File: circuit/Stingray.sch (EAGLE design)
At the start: 14 parts, among them IC1 4052N, IC2 4052N, K1 5200, K3 PN87520-S, M1 ARDUINO-NANO-3.0

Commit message: added files via upload
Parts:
- added R6, R7, R8: 10k, rcl:R-EU_0204/7
- added X2: (no value), con-yamaichi:MD06SS
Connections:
- removed net TXD/SPARE: M1.D1/TX
- new net PS2CLK: M1.D1/TX, R6.2, X2.5
- new net PS2DAT: M1.D0/RX, R7.2, X2.1
- net +5V: now also R6.1, R7.1, R8.2, X2.4
- net DETECT: now also M1.A6, R8.1; no longer M1.D0/RX
- net GND: now also X2.3
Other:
- moved on the sheet: K2, K3

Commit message: Alpha release, Joystick control seems fine, keyboard emulation to be tested.
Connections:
- net BOTTOM: now also K1.13, M1.D3; no longer K1.14, M1.D2
- net TOP: now also K1.14, M1.D2; no longer K1.13, M1.D3
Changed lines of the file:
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@@
 <grid distance="0.1" unitdist="inch" unit="inch" style="lines" multiple="1" display="no" altdistance="0.01" altunitdist="inch" altunit="inch"/>
 <layers>
-<layer number="1" name="Top" color="4" fill="1" visible="yes" active="no"/>
-<layer number="16" name="Bottom" color="1" fill="1" visible="yes" active="no"/>
-<layer number="17" name="Pads" color="2" fill="1" visible="yes" active="no"/>
-<layer number="18" name="Vias" color="2" fill="1" visible="yes" active="no"/>
-<layer number="19" name="Unrouted" color="6" fill="1" visible="yes" active="no"/>
-<layer number="20" name="Dimension" color="15" fill="1" visible="yes" active="no"/>
-<layer number="21" name="tPlace" color="7" fill="1" visible="yes" active="no"/>
-<layer number="22" name="bPlace" color="7" fill="1" visible="yes" active="no"/>
-<layer number="23" name="tOrigins" color="15" fill="1" visible="yes" active="no"/>
-<layer number="24" name="bOrigins" color="15" fill="1" visible="yes" active="no"/>
-<layer number="25" name="tNames" color="7" fill="1" visible="yes" active="no"/>
-<layer number="26" name="bNames" color="7" fill="1" visible="yes" active="no"/>
-<layer number="27" name="tValues" color="7" fill="1" visible="yes" active="no"/>
-<layer number="28" name="bValues" color="7" fill="1" visible="yes" active="no"/>
+<layer number="1" name="Top" color="4" fill="1" visible="no" active="no"/>
+<layer number="16" name="Bottom" color="1" fill="1" visible="no" active="no"/>
+<layer number="17" name="Pads" color="2" fill="1" visible="no" active="no"/>
+<layer number="18" name="Vias" color="2" fill="1" visible="no" active="no"/>
+<layer number="19" name="Unrouted" color="6" fill="1" visible="no" active="no"/>
+<layer number="20" name="Dimension" color="15" fill="1" visible="no" active="no"/>
+<layer number="21" name="tPlace" color="7" fill="1" visible="no" active="no"/>
+<layer number="22" name="bPlace" color="7" fill="1" visible="no" active="no"/>
+<layer number="23" name="tOrigins" color="15" fill="1" visible="no" active="no"/>
+<layer number="24" name="bOrigins" color="15" fill="1" visible="no" active="no"/>
+<layer number="25" name="tNames" color="7" fill="1" visible="no" active="no"/>
+<layer number="26" name="bNames" color="7" fill="1" visible="no" active="no"/>
+<layer number="27" name="tValues" color="7" fill="1" visible="no" active="no"/>
+<layer number="28" name="bValues" color="7" fill="1" visible="no" active="no"/>
 <layer number="29" name="tStop" color="7" fill="3" visible="no" active="no"/>
 <layer number="30" name="bStop" color="7" fill="6" visible="no" active="no"/>
@@
 <layer number="35" name="tGlue" color="7" fill="4" visible="no" active="no"/>
 <layer number="36" name="bGlue" color="7" fill="5" visible="no" active="no"/>
-<layer number="37" name="tTest" color="7" fill="1" visible="yes" active="no"/>
-<layer number="38" name="bTest" color="7" fill="1" visible="yes" active="no"/>
+<layer number="37" name="tTest" color="7" fill="1" visible="no" active="no"/>
+<layer number="38" name="bTest" color="7" fill="1" visible="no" active="no"/>
 <layer number="39" name="tKeepout" color="4" fill="11" visible="no" active="no"/>
 <layer number="40" name="bKeepout" color="1" fill="11" visible="no" active="no"/>
@@
 <layer number="44" name="Drills" color="7" fill="1" visible="no" active="no"/>
 <layer number="45" name="Holes" color="7" fill="1" visible="no" active="no"/>
-<layer number="46" name="Milling" color="3" fill="1" visible="yes" active="no"/>
-<layer number="47" name="Measures" color="7" fill="1" visible="yes" active="no"/>
-<layer number="48" name="Document" color="7" fill="1" visible="yes" active="no"/>
-<layer number="49" name="Reference" color="7" fill="1" visible="yes" active="no"/>
-<layer number="50" name="dxf" color="7" fill="1" visible="yes" active="no"/>
-<layer number="51" name="tDocu" color="7" fill="1" visible="yes" active="no"/>
-<layer number="52" name="bDocu" color="7" fill="1" visible="yes" active="no"/>
-<layer number="53" name="tGND_GNDA" color="7" fill="9" visible="yes" active="no"/>
-<layer number="54" name="bGND_GNDA" color="1" fill="9" visible="yes" active="no"/>
-<layer number="56" name="wert" color="7" fill="1" visible="yes" active="no"/>
-<layer number="57" name="tCAD" color="7" fill="1" visible="yes" active="no"/>
-<layer number="59" name="tCarbon" color="7" fill="1" visible="yes" active="no"/>
-<layer number="60" name="bCarbon" color="7" fill="1" visible="yes" active="no"/>
+<layer number="46" name="Milling" color="3" fill="1" visible="no" active="no"/>
+<layer number="47" name="Measures" color="7" fill="1" visible="no" active="no"/>
+<layer number="48" name="Document" color="7" fill="1" visible="no" active="no"/>
+<layer number="49" name="Reference" color="7" fill="1" visible="no" active="no"/>
+<layer number="50" name="dxf" color="7" fill="1" visible="no" active="no"/>
+<layer number="51" name="tDocu" color="7" fill="1" visible="no" active="no"/>
+<layer number="52" name="bDocu" color="7" fill="1" visible="no" active="no"/>
+<layer number="53" name="tGND_GNDA" color="7" fill="9" visible="no" active="no"/>
+<layer number="54" name="bGND_GNDA" color="1" fill="9" visible="no" active="no"/>
+<layer number="56" name="wert" color="7" fill="1" visible="no" active="no"/>
+<layer number="57" name="tCAD" color="7" fill="1" visible="no" active="no"/>
+<layer number="59" name="tCarbon" color="7" fill="1" visible="no" active="no"/>
+<layer number="60" name="bCarbon" color="7" fill="1" visible="no" active="no"/>
 <layer number="90" name="Modules" color="5" fill="1" visible="yes" active="yes"/>
 <layer number="91" name="Nets" color="2" fill="1" visible="yes" active="yes"/>
@@
 </segment>
 </net>
-<net name="BOTTOM" class="0">
+<net name="TOP" class="0">
 <segment>
 <pinref part="K1" gate="-1" pin="14"/>
@@
 </segment>
 </net>
-<net name="TOP" class="0">
+<net name="BOTTOM" class="0">
 <segment>
 <wire x1="139.7" y1="106.68" x2="160.02" y2="106.68" width="0.1524" layer="91"/>

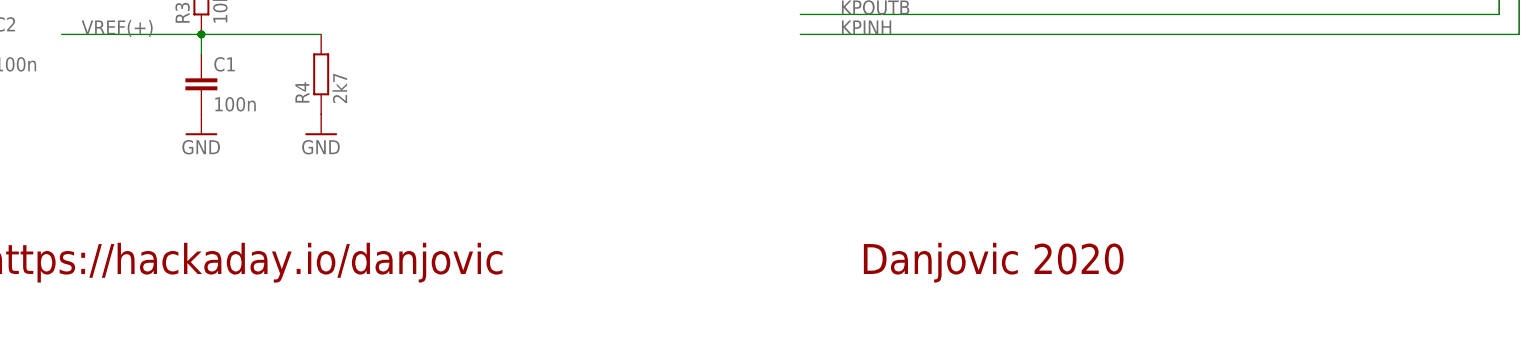
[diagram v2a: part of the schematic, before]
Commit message: Corrected mirrored Wii connector footprint
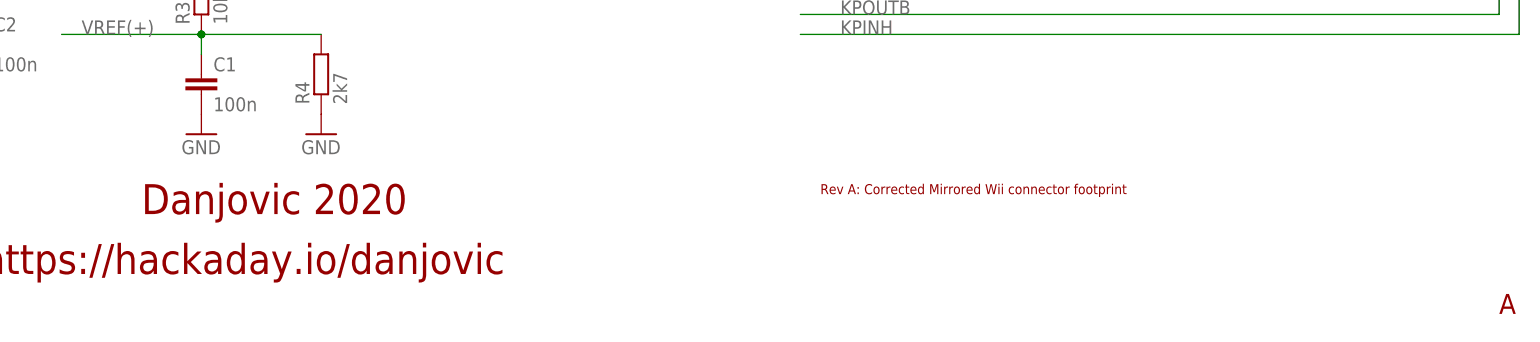
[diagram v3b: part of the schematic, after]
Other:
- note added: "A"
- note added: "Rev A: Corrected Mirrored Wii connector footprint"
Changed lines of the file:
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@@
 <plain>
 <text x="127" y="162.56" size="5.08" layer="94" font="vector" ratio="13" align="center">Wii Classic Controller adapter for Atari 5200</text>
-<text x="167.64" y="10.16" size="3.81" layer="94" font="vector" ratio="13">Danjovic 2020</text>
+<text x="76.2" y="17.78" size="3.81" layer="94" font="vector" ratio="13">Danjovic 2020</text>
 <text x="55.88" y="10.16" size="3.81" layer="94" font="vector" ratio="13">https://hackaday.io/danjovic</text>
+<text x="248.92" y="5.08" size="2.54" layer="94">A</text>
+<text x="162.56" y="20.32" size="1.27" layer="94" font="vector">Rev A: Corrected Mirrored Wii connector footprint</text>
 </plain>
 <instances>

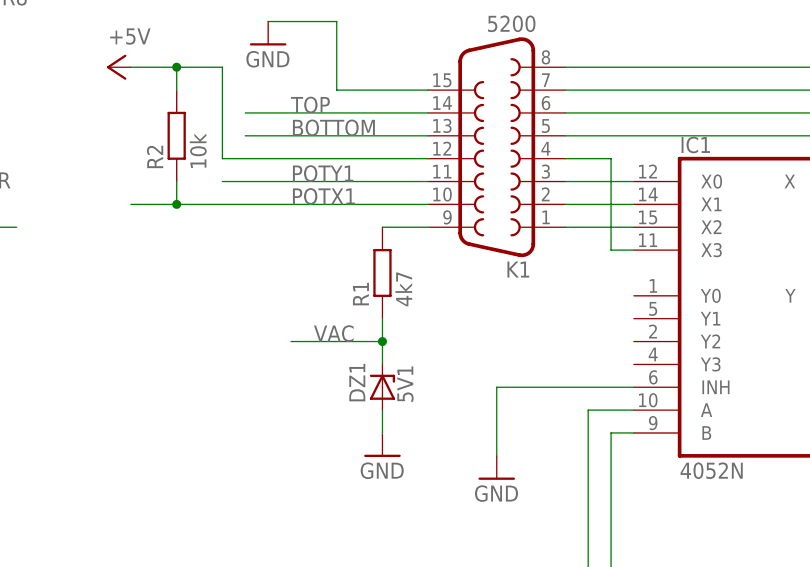
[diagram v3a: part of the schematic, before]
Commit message: Updated value of R1 to 1K
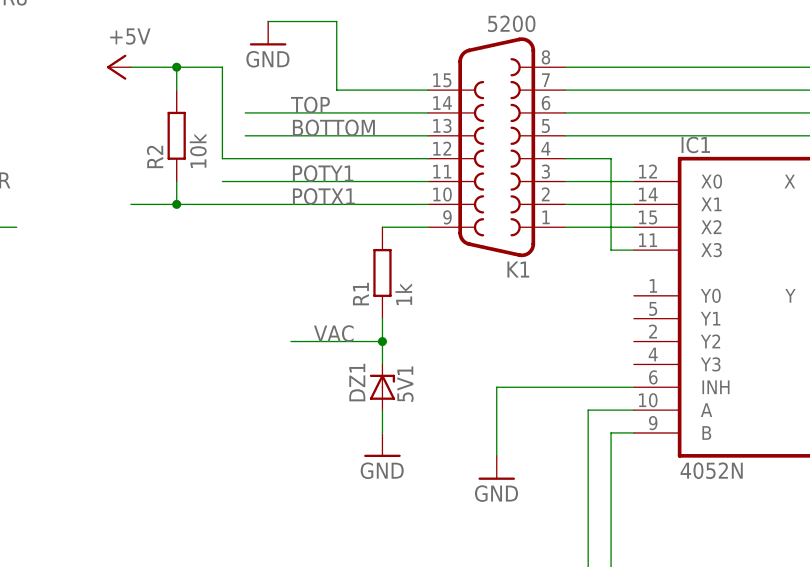
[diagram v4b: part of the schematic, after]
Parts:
- R1: value 4k7 -> 1k
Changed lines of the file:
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@@
 <?xml version="1.0" encoding="utf-8"?>
 <!DOCTYPE eagle SYSTEM "eagle.dtd">
-<eagle version="7.2.0">
+<eagle version="6.5.0">
 <drawing>
 <settings>
@@
 <part name="P+2" library="supply1" deviceset="+5V" device=""/>
 <part name="P+6" library="supply1" deviceset="+5V" device=""/>
-<part name="R1" library="rcl" deviceset="R-EU_" device="0204/7" value="4k7"/>
+<part name="R1" library="rcl" deviceset="R-EU_" device="0204/7" value="1k"/>
 <part name="IC1" library="40xx" deviceset="4052" device="N"/>
 <part name="IC2" library="40xx" deviceset="4052" device="N"/>
